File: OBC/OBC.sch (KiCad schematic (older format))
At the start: 3 parts, among them J0 Raspberry_Pi_2_3, J1 Power, U0 Payload

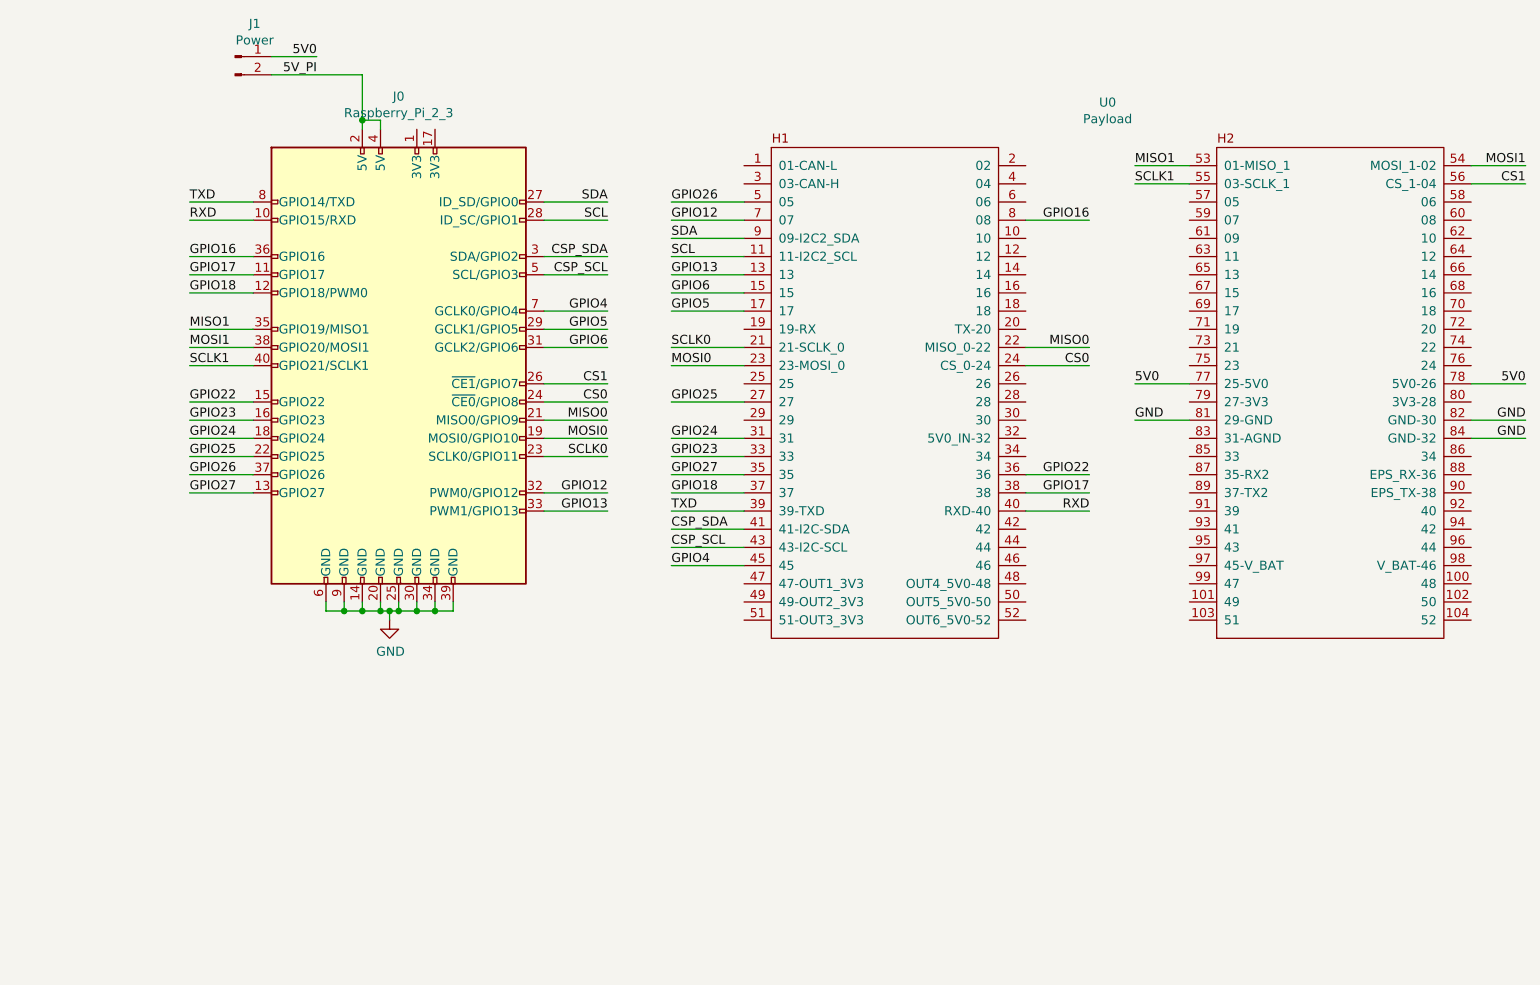
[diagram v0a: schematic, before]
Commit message: Added output connectors. They consist on power outputs through a terminal block and two picoblades, and I2C pin headers.
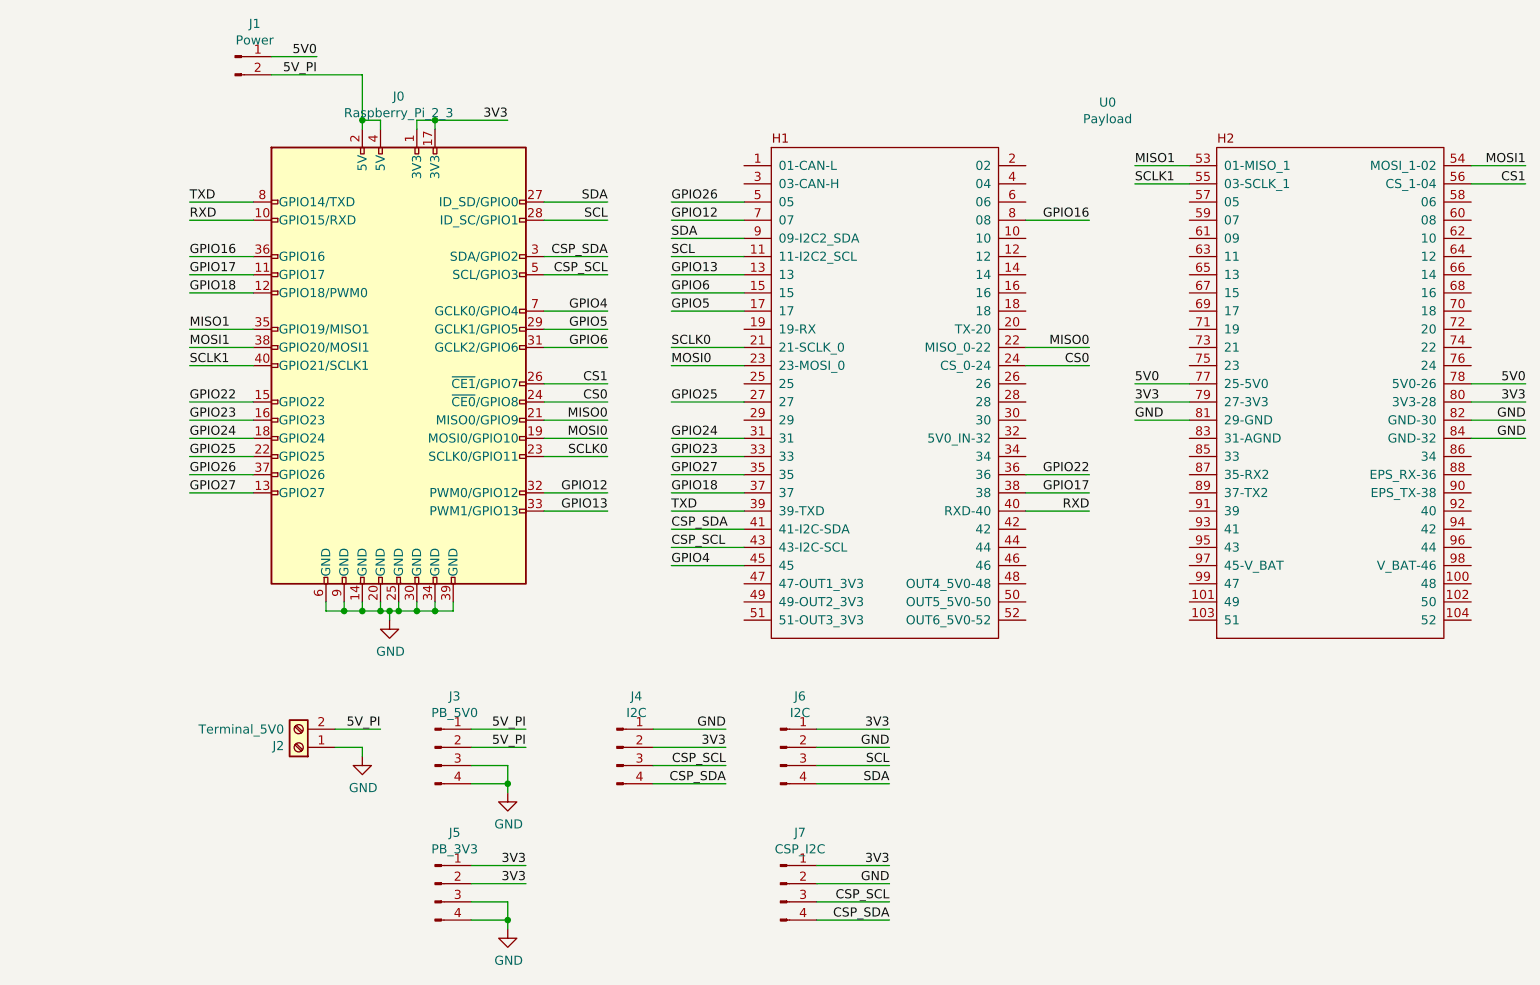
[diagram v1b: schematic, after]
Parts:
- added J2: Terminal_5V0, TerminalBlock:TerminalBlock_Altech_AK300-2_P5.00mm, symbol Connector:Screw_Terminal_01x02
- added J3: PB_5V0, Connector_Molex:Molex_PicoBlade_53048-0410_1x04_P1.25mm_Horizontal, symbol Connector:Conn_01x04_Male
- added J4, J6: I2C, Connector_PinHeader_2.54mm:PinHeader_1x04_P2.54mm_Vertical, symbol Connector:Conn_01x04_Male
- added J5: PB_3V3, Connector_Molex:Molex_PicoBlade_53048-0410_1x04_P1.25mm_Horizontal, symbol Connector:Conn_01x04_Male
- added J7: CSP_I2C, Connector_PinHeader_2.54mm:PinHeader_1x04_P2.54mm_Vertical, symbol Connector:Conn_01x04_Male
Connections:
- net 5V_PI: now also J2.2 (Pin_2), J3.1 (Pin_1), J3.2 (Pin_2)
- net CSP_SCL: now also J4.3 (Pin_3), J7.3 (Pin_3)
- net CSP_SDA: now also J4.4 (Pin_4), J7.4 (Pin_4)
- net GND: now also J2.1 (Pin_1), J3.3 (Pin_3), J3.4 (Pin_4), J4.1 (Pin_1), J5.3 (Pin_3), J5.4 (Pin_4), J6.2 (Pin_2), J7.2 (Pin_2)
- net SCL: now also J6.3 (Pin_3)
- net SDA: now also J6.4 (Pin_4)
- net 3V3: now reaches U0.79 (27-3V3)
- net 3V3: now also J0.1 (3V3), J0.17 (3V3), U0.80 (3V3-28), J4.2 (Pin_2), J5.1 (Pin_1), J5.2 (Pin_2), J6.1 (Pin_1), J7.1 (Pin_1)
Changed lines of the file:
@@
 EESchema Schematic File Version 5
+LIBS:OBC-cache
 EELAYER 29 0
 EELAYER END
@@
 Wire Wire Line
 	7950 2200 7600 2200
+Wire Wire Line
+	8200 3200 8500 3200
+Wire Wire Line
+	10350 3200 10050 3200
+Text Label 8200 3200 0    50   ~ 0
+3V3
+Text Label 10350 3200 2    50   ~ 0
+3V3
+Wire Wire Line
+	4250 1700 4250 1650
+Wire Wire Line
+	4250 1650 4350 1650
+Wire Wire Line
+	4350 1650 4350 1700
+Wire Wire Line
+	4350 1650 4750 1650
+Connection ~ 4350 1650
+Text Label 4750 1650 2    50   ~ 0
+3V3
+$Comp
+L Connector:Screw_Terminal_01x02 J2
+U 1 1 5D261C4A
+P 3600 5100
+F 0 "J2" H 3680 5092 50  0000 L CNN
+F 1 "Terminal_5V0" H 3680 5001 50  0000 L CNN
+F 2 "TerminalBlock:TerminalBlock_Altech_AK300-2_P5.00mm" H 3600 5100 50  0001 C CNN
+F 3 "~" H 3600 5100 50  0001 C CNN
+	1    3600 5100
+	-1   0    0    1
+$EndComp
+$Comp
+L Connector:Conn_01x04_Male J3
+U 1 1 5D262D74
+P 4350 5100
+F 0 "J3" H 4458 5381 50  0000 C CNN
+F 1 "PB_5V0" H 4458 5290 50  0000 C CNN
+F 2 "Connector_Molex:Molex_PicoBlade_53048-0410_1x04_P1.25mm_Horizontal" H 4350 5100 50  0001 C CNN
+F 3 "~" H 4350 5100 50  0001 C CNN
+	1    4350 5100
+	1    0    0    -1
+$EndComp
+$Comp
+L Connector:Conn_01x04_Male J6
+U 1 1 5D2667C7
+P 6250 5100
+F 0 "J6" H 6358 5381 50  0000 C CNN
+F 1 "I2C" H 6358 5290 50  0000 C CNN
+F 2 "Connector_PinHeader_2.54mm:PinHeader_1x04_P2.54mm_Vertical" H 6250 5100 50  0001 C CNN
+F 3 "~" H 6250 5100 50  0001 C CNN
+	1    6250 5100
+	1    0    0    -1
+$EndComp
+$Comp
+L Connector:Conn_01x04_Male J7
+U 1 1 5D266E04
+P 6250 5850
+F 0 "J7" H 6358 6131 50  0000 C CNN
+F 1 "CSP_I2C" H 6358 6040 50  0000 C CNN
+F 2 "Connector_PinHeader_2.54mm:PinHeader_1x04_P2.54mm_Vertical" H 6250 5850 50  0001 C CNN
+F 3 "~" H 6250 5850 50  0001 C CNN
+	1    6250 5850
+	1    0    0    -1
+$EndComp
+Text Label 4050 5000 2    50   ~ 0
+5V_PI
+Text Label 4850 5000 2    50   ~ 0
+5V_PI
+Text Label 4850 5100 2    50   ~ 0
+5V_PI
+Text Label 4850 5750 2    50   ~ 0
+3V3
+Text Label 4850 5850 2    50   ~ 0
+3V3
+Wire Wire Line
+	4050 5000 3800 5000
+Wire Wire Line
+	3800 5100 3950 5100
+Wire Wire Line
+	3950 5100 3950 5150
+$Comp
+L power:GND #PWR0102
+U 1 1 5D2690FB
+P 3950 5150
+F 0 "#PWR0102" H 3950 4900 50  0001 C CNN
+F 1 "GND" H 3955 4977 50  0000 C CNN
+F 2 "" H 3950 5150 50  0001 C CNN
+F 3 "" H 3950 5150 50  0001 C CNN
+	1    3950 5150
+	1    0    0    -1
+$EndComp
+Wire Wire Line
+	4850 5000 4550 5000
+Wire Wire Line
+	4550 5100 4850 5100
+Wire Wire Line
+	4850 5750 4550 5750
+Wire Wire Line
+	4550 5850 4850 5850
+Wire Wire Line
+	4550 5300 4750 5300
+Wire Wire Line
+	4750 5300 4750 5350
+Wire Wire Line
+	4550 5200 4750 5200
+Wire Wire Line
+	4750 5200 4750 5300
+Connection ~ 4750 5300
+Wire Wire Line
+	4550 5950 4750 5950
+Wire Wire Line
+	4750 5950 4750 6050
+Wire Wire Line
+	4550 6050 4750 6050
+Connection ~ 4750 6050
+Wire Wire Line
+	4750 6050 4750 6100
+$Comp
+L power:GND #PWR0104
+U 1 1 5D26A2CE
+P 4750 5350
+F 0 "#PWR0104" H 4750 5100 50  0001 C CNN
+F 1 "GND" H 4755 5177 50  0000 C CNN
+F 2 "" H 4750 5350 50  0001 C CNN
+F 3 "" H 4750 5350 50  0001 C CNN
+	1    4750 5350
+	1    0    0    -1
+$EndComp
+$Comp
+L power:GND #PWR0105
+U 1 1 5D26A590
+P 4750 6100
+F 0 "#PWR0105" H 4750 5850 50  0001 C CNN
+F 1 "GND" H 4755 5927 50  0000 C CNN
+F 2 "" H 4750 6100 50  0001 C CNN
+F 3 "" H 4750 6100 50  0001 C CNN
+	1    4750 6100
+	1    0    0    -1
+$EndComp
+Text Label 6850 6050 2    50   ~ 0
+CSP_SDA
+Text Label 6850 5950 2    50   ~ 0
+CSP_SCL
+Text Label 6850 5300 2    50   ~ 0
+SDA
+Text Label 6850 5200 2    50   ~ 0
+SCL
+Text Label 6850 5000 2    50   ~ 0
+3V3
+Text Label 6850 5750 2    50   ~ 0
+3V3
+Wire Wire Line
+	6850 5000 6450 5000
+Wire Wire Line
+	6450 5100 6850 5100
+Wire Wire Line
+	6850 5200 6450 5200
+Wire Wire Line
+	6850 5750 6450 5750
+Wire Wire Line
+	6450 5850 6850 5850
+Wire Wire Line
+	6850 5950 6450 5950
+$Comp
+L Connector:Conn_01x04_Male J5
+U 1 1 5D266258
+P 4350 5850
+F 0 "J5" H 4458 6131 50  0000 C CNN
+F 1 "PB_3V3" H 4458 6040 50  0000 C CNN
+F 2 "Connector_Molex:Molex_PicoBlade_53048-0410_1x04_P1.25mm_Horizontal" H 4350 5850 50  0001 C CNN
+F 3 "~" H 4350 5850 50  0001 C CNN
+	1    4350 5850
+	1    0    0    -1
+$EndComp
+Wire Wire Line
+	6450 6050 6850 6050
+Wire Wire Line
+	6450 5300 6850 5300
+Text Label 6850 5100 2    50   ~ 0
+GND
+Text Label 6850 5850 2    50   ~ 0
+GND
+Text Label 5950 5000 2    50   ~ 0
+GND
+Wire Wire Line
+	5550 5300 5950 5300
+Text Label 5950 5100 2    50   ~ 0
+3V3
+$Comp
+L Connector:Conn_01x04_Male J4
+U 1 1 5D2773BC
+P 5350 5100
+F 0 "J4" H 5458 5381 50  0000 C CNN
+F 1 "I2C" H 5458 5290 50  0000 C CNN
+F 2 "Connector_PinHeader_2.54mm:PinHeader_1x04_P2.54mm_Vertical" H 5350 5100 50  0001 C CNN
+F 3 "~" H 5350 5100 50  0001 C CNN
+	1    5350 5100
+	1    0    0    -1
+$EndComp
+Wire Wire Line
+	5950 5200 5550 5200
+Text Label 5950 5300 2    50   ~ 0
+CSP_SDA
+Text Label 5950 5200 2    50   ~ 0
+CSP_SCL
+Wire Wire Line
+	5550 5100 5950 5100
+Wire Wire Line
+	5950 5000 5550 5000
 $EndSCHEMATC
